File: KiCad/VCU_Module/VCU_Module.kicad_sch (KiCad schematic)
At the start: 46 parts, among them J1 5810132011, J10 12V, J12 MCU1, J13 MCU2, J14 5V, J15 3V3, J16 MCU3, J17 MCU4, J2 CN1, J3 CN2, J4 CN3, J5 MCU6, J6 CN4, J7 MCU5, J9 GND, Q1 SUD19P06-60, U3 LMR33640DDDA, U4 LMR33640DDDA

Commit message: updated pcb from sohams adjustments to schematic
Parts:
- removed S1: 100SP1T1B4M2QE, VMS_Footprints:SW_100SP1T1B4M2QE, symbol 100SP1T1B4M2QE:100SP1T1B4M2QE
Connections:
- net at CR1.1, Q1.3 (S): now also F1.1
- net +3V3 renamed 3V3
- net +5V renamed 5V
- net MCU/PA5/SPI1_SCK renamed MCU/PA5/User LED 1
- net MCU/PC9/TIM1_CH2 renamed MCU/PC9/User LED 2
- no-connect marks 3 -> 2
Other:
- sheet MCU ports: added PA5/User LED 1, PC9/User LED 2; removed PA5/SPI1_SCK, PC9/TIM1_CH2
- moved on the sheet: F1

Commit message: notes for changes from andrew
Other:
- note added: "specify in the chematic what is the fuse, what is the part number, change to fuse holder and fuse, maybe ptc fuse. probably smd holder and fuse smallest i can find change user leds remove transistor, move them next c13 between reset and ground, double check data sheet double check pa2 and pa3 are wired correctly double check pa13 and pa14 reroute traces and get pcb finalized"
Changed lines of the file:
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@@
+		)
+	)
+	(text "specify in the chematic what is the fuse, what is the part number, change to fuse holder and fuse, maybe ptc fuse. probably smd holder and fuse smallest i can find\n\nchange user leds remove transistor, move them next \n\nc13 between reset and ground, double check data sheet\n\ndouble check pa2 and pa3 are wired correctly\n\ndouble check pa13 and pa14\n\nreroute traces and get pcb finalized\n\n\n\n\n"
+		(exclude_from_sim no)
+		(at 233.68 97.536 0)
+		(effects
+			(font
+				(size 1.27 1.27)
+			)
 		)
 	)

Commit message: schematic complete with new fuse holder and specs, just need to run ERC once more PCB component placement and traces done, still need to fix some DRC Errors and check warnings Still need to ensure all components are labeled properly with no overlapping silkscreen labels
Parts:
- removed F1: Fuse, Fuse:Fuse_1206_3216Metric, symbol Device:Fuse
- removed J1: 5810132011, VMS_Footprints:CINCH_5810132011_30-pin, symbol CINCH5810132011:5810132011
- added F1: 3568, VMS_Footprints:FUSE_3568, symbol VMS_Symbols:3568
- added J1: 5810132011, VMS_Footprints:Cinch_5810132011_PCB_Header, symbol Cinch_5810132011_PCB_Header:5810132011
- J10: symbol Connector:Conn_01x02_Socket -> Connector_Generic:Conn_01x02
- J12, J13, J16, J17, J2, J3: symbol Connector:Conn_01x10_Socket -> Connector_Generic:Conn_01x10
- J14, J15, J5, J9: symbol Connector:Conn_01x04_Socket -> Connector_Generic:Conn_01x04
- J4, J6, J7: symbol Connector:Conn_01x06_Socket -> Connector_Generic:Conn_01x06
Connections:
- net VDD: now also F1.2, F1.4
- net VIN_PROTECTED: now also CR1.1, Q1.3 (S); no longer Q1.2 (D)
- net at J3.1 (Pin_1): now also J1.A11
- net at J3.10 (Pin_10): now also J1.A20
- net at J3.2 (Pin_2): now also J1.A12
- net at J3.3 (Pin_3): now also J1.A13
- net at J3.4 (Pin_4): now also J1.A14
- net at J3.5 (Pin_5): now also J1.A15
- net at J3.6 (Pin_6): now also J1.A16
- net at J3.7 (Pin_7): now also J1.A17
- net at J3.8 (Pin_8): now also J1.A18
- net at J3.9 (Pin_9): now also J1.A19
- net at J6.1 (Pin_1): now also J1.B7
- net at J6.2 (Pin_2): now also J1.B8
- net at J6.3 (Pin_3): now also J1.B9
- net at J6.4 (Pin_4): now also J1.B10
- net at J6.5 (Pin_5): now also J1.B11
- net at J6.6 (Pin_6): now also J1.B12
- net at J2.1 (Pin_1): now also J1.A1
- net at J2.10 (Pin_10): now also J1.A10
- net at J2.2 (Pin_2): now also J1.A2
- net at J2.3 (Pin_3): now also J1.A3
- net at J2.4 (Pin_4): now also J1.A4
- net at J2.5 (Pin_5): now also J1.A5
- net at J2.6 (Pin_6): now also J1.A6
- net at J2.7 (Pin_7): now also J1.A7
- net at J2.8 (Pin_8): now also J1.A8
- net at J2.9 (Pin_9): now also J1.A9
- net at J4.1 (Pin_1): now also J1.B1
- net at J4.2 (Pin_2): now also J1.B2
- net at J4.3 (Pin_3): now also J1.B3
- net at J4.4 (Pin_4): now also J1.B4
- net at J4.5 (Pin_5): now also J1.B5
- net at J4.6 (Pin_6): now also J1.B6
- new net: F1.1, F1.3, Q1.2 (D)
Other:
- note added: "Mini automotive blade fuse, 1A - 3A depending on application 36V rated"
- note removed: "specify in the chematic what is the fuse, what is the part number, change to fuse holder and fuse, maybe ptc fuse. probably smd holder and fuse smallest i can find change user leds remove transistor, move them next c13 between reset and ground, double check data sheet double check pa2 and pa3 are wired correctly double check pa13 and pa14 reroute traces and get pcb finalized"
- moved on the sheet: J10

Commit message: finished DRC checks and ERC checks in schematic and PCB, added many new components with purchase links to BOM, still need to double check previously added parts in BOM to ensure they are sufficient for higher voltage inputs
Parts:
- C11, C4: DPN 311-1869-1-ND -> 1276-7012-1-ND; MFR YAGEO -> Samsung Electro-Mechanics; MPN CC0805KKX5R8BB106 -> CL21B224KBFVPNE; Purchase Link https://www.digikey.com/en/products/detail/yageo/CC0805KKX5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 -> https://www.digikey.com/en/products/detail/samsung-electro-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
- C12, C18, C19, C20, C21, C5, C6, C7, C8, C9: DIS DigiKey -> (none); DPN 311-1869-1-ND -> (none); MFR YAGEO -> (none); MPN CC0805KKX5R8BB106 -> (none); Purchase Link https://www.digikey.com/en/products/detail/yageo/CC0805KKX5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 -> (none)
- CR1: DPN MMSZ5245B-FDICT-ND -> 3757-MMSZ5240B_R1_00001CT-ND; MFR Diodes Incorporated -> Panjit International Inc.; MPN MMSZ5240B -> MMSZ5240B_R1_00001; Purchase Link (none) -> https://www.digikey.com/en/products/detail/panjit-internati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
- F1: DIS (none) -> DigiKey; DPN (none) -> 36-3568-ND; MFR (none) -> Keystone Electronics; MPN (none) -> 3568; Purchase Link (none) -> https://www.digikey.com/en/products/detail/keystone-electro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
- J1: DIS (none) -> DigiKey; DPN (none) -> 116-1124-ND; MFR (none) -> Cinch Connectivity Solutions; MPN (none) -> 5810132011; Purchase Link (none) -> https://www.digikey.com/en/products/detail/cinch-connectivi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
- J12, J13, J16, J17, J2, J3: DIS (none) -> DigiKey; DPN (none) -> S7043-ND; MFR (none) -> Sullins Connector Solutions; MPN (none) -> PPPC101LFBN-RC; Purchase Link (none) -> https://www.digikey.com/en/products/detail/sullins-connecto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
- J4, J5, J6, J7: DIS (none) -> DigiKey; DPN (none) -> S7039-ND; MFR (none) -> Sullins Connector Solutions; MPN (none) -> PPPC061LFBN-RC; Purchase Link (none) -> https://www.digikey.com/en/products/detail/sullins-connecto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
- L1, L2: DIS (none) -> DigiKey; DPN (none) -> 1712-7-2176797-0CT-ND; MFR (none) -> TE Connectivity Passive Product; MPN (none) -> 7-2176797-0; Purchase Link (none) -> https://www.digikey.com/en/products/detail/te-connectivity-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
- Q1: DIS (none) -> DigiKey; DPN (none) -> SUD19P06-60-GE3CT-ND; MFR (none) -> Vishay Siliconix; MPN (none) -> SUD19P06-60-GE3; Purchase Link (none) -> https://www.digikey.com/en/products/detail/vishay-siliconix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
- U3, U4: DIS (none) -> DigiKey; DPN (none) -> 296-LMR33640DDDARCT-ND; MFR (none) -> Texas Instruments; MPN (none) -> LMR33640DDDAR; Purchase Link (none) -> https://www.digikey.com/en/products/detail/texas-instrument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

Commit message: finalized BOM
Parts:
- C10, C3: DPN 311-1869-1-ND -> 490-12394-1-ND; MFR YAGEO -> Murata Electronics; MPN CC0805KKX5R8BB106 -> GRT21BR61H475KE13L; Purchase Link https://www.digikey.com/en/products/detail/yageo/CC0805KKX5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 -> https://www.digikey.com/en/products/detail/murata-electroni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
- C12, C9: DIS (none) -> DigiKey; DPN (none) -> 445-6974-1-ND; MFR (none) -> TDK; MPN (none) -> CGA4J3X7S2A105K125AB; Purchase Link (none) -> https://www.digikey.com/en/products/detail/tdk/CGA4J3X7S2A1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
- C18, C5: DIS (none) -> DigiKey; DPN (none) -> 490-5825-1-ND; MFR (none) -> Murata Electronics; MPN (none) -> GCJ21BR72A104KA01L; Purchase Link (none) -> https://www.digikey.com/en/products/detail/murata-electroni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
- C19, C20, C21, C6, C7, C8: DIS (none) -> DigiKey; DPN (none) -> 4713-GMC21X5R226K16NTCT-ND; MFR (none) -> Cal-Chip Electronics, Inc.; MPN (none) -> GMC21X5R226K16NT; Purchase Link (none) -> https://www.digikey.com/en/products/detail/cal-chip-electro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
- J10: DPN S1011EC-02-ND -> S7035-ND; MPN PRPC002SAAN-RC -> PPPC021LFBN-RC; Purchase Link https://www.digikey.com/en/products/detail/sullins-connector-solutions/PRPC002SAAN-RC/2775252 -> https://www.digikey.com/en/products/detail/sullins-connector-solutions/PPPC021LFBN-RC/810174
- J14, J15, J9: DPN S1011EC-04-ND -> S7037-ND; MPN PRPC004SAAN-RC -> PPPC041LFBN-RC; Purchase Link https://www.digikey.com/en/products/detail/sullins-connector-solutions/PRPC004SAAN-RC/2775250 -> https://www.digikey.com/en/products/detail/sullins-connector-solutions/PPPC041LFBN-RC/810176
- J5: DPN S7039-ND -> S7037-ND; MPN PPPC061LFBN-RC -> PPPC041LFBN-RC; Purchase Link https://www.digikey.com/en/products/detail/sullins-connector-solutions/PPPC061LFBN-RC/810178 -> https://www.digikey.com/en/products/detail/sullins-connector-solutions/PPPC041LFBN-RC/810176
- R1: DPN 311-100KCRCT-ND -> 2019-SG73S2ATTD1003FCT-ND; MFR YAGEO -> KOA Speer Electronics, Inc.; MPN RC0805FR-07100KL -> SG73S2ATTD1003F; Purchase Link https://www.digikey.com/en/products/detail/yageo/RC0805FR-0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 -> https://www.digikey.com/en/products/detail/koa-speer-electr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
- R2, R8: DPN 311-1.00KCRCT-ND -> 2019-SG73S2ATTD1001FCT-ND; MFR YAGEO -> KOA Speer Electronics, Inc.; MPN RC0805FR-071KL -> SG73S2ATTD1001F; Purchase Link https://www.digikey.com/en/products/detail/yageo/RC0805FR-0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 -> https://www.digikey.com/en/products/detail/koa-speer-electr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
- R4, R6: DPN 311-1.00KCRCT-ND -> 2019-SG73S2ATTD1003FCT-ND; MFR YAGEO -> KOA Speer Electronics, Inc.; MPN RC0805FR-071KL -> SG73S2ATTD1003F; Purchase Link https://www.digikey.com/en/products/detail/yageo/RC0805FR-0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 -> https://www.digikey.com/en/products/detail/koa-speer-electr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
- R5: DPN 311-1.00KCRCT-ND -> 2019-RK73H2ATTD4322FCT-ND; MFR YAGEO -> KOA Speer Electronics, Inc.; MPN RC0805FR-071KL -> RK73H2ATTD4322F; Purchase Link https://www.digikey.com/en/products/detail/yageo/RC0805FR-0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 -> https://www.digikey.com/en/products/detail/koa-speer-electr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
- R7: DPN 311-1.00KCRCT-ND -> 2019-RK73H2ATTD2492FCT-ND; MFR YAGEO -> KOA Speer Electronics, Inc.; MPN RC0805FR-071KL -> RK73H2ATTD2492F; Purchase Link https://www.digikey.com/en/products/detail/yageo/RC0805FR-0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 -> https://www.digikey.com/en/products/detail/koa-speer-electr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

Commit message: final PCB fix
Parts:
- removed CR1: MMSZ5240B, VMS_Footprints:SOD123_DIO, symbol MMSZ5245B_7_F:MMSZ5245B-7-F
- added CR1: MMSZ5245B-7-F, VMS_Footprints:SOD123_DIO, symbol VMS_Symbols:MMSZ5245B-7-F
- added F2: 1A, symbol Device:Fuse
- added J18: Molex MX150 12_pin, N/A, symbol Connector_Generic:Conn_02x06_Counter_Clockwise
- added J19: Molex MX150 20_pin, N/A, symbol Connector_Generic:Conn_02x10_Counter_Clockwise
- added N1: Cinch 5810130065 Enclosure, N/A, symbol Mechanical:Housing
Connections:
- net VIN_PROTECTED: now also CR1.1
- net at Q1.1 (G), R1.1: now also CR1.2
- no-connect marks 2 -> 36
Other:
- note added: "Miniature blade fuse"

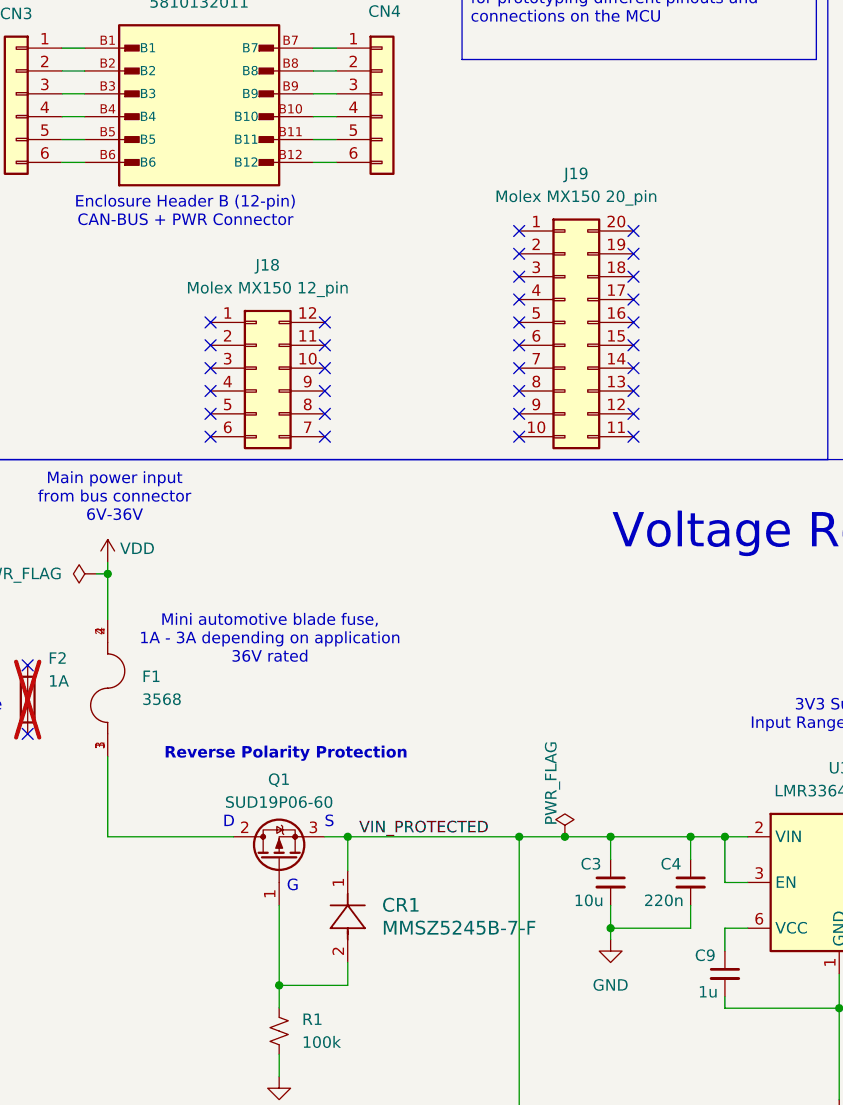
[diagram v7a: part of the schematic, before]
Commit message: updating components with AEC certified ones
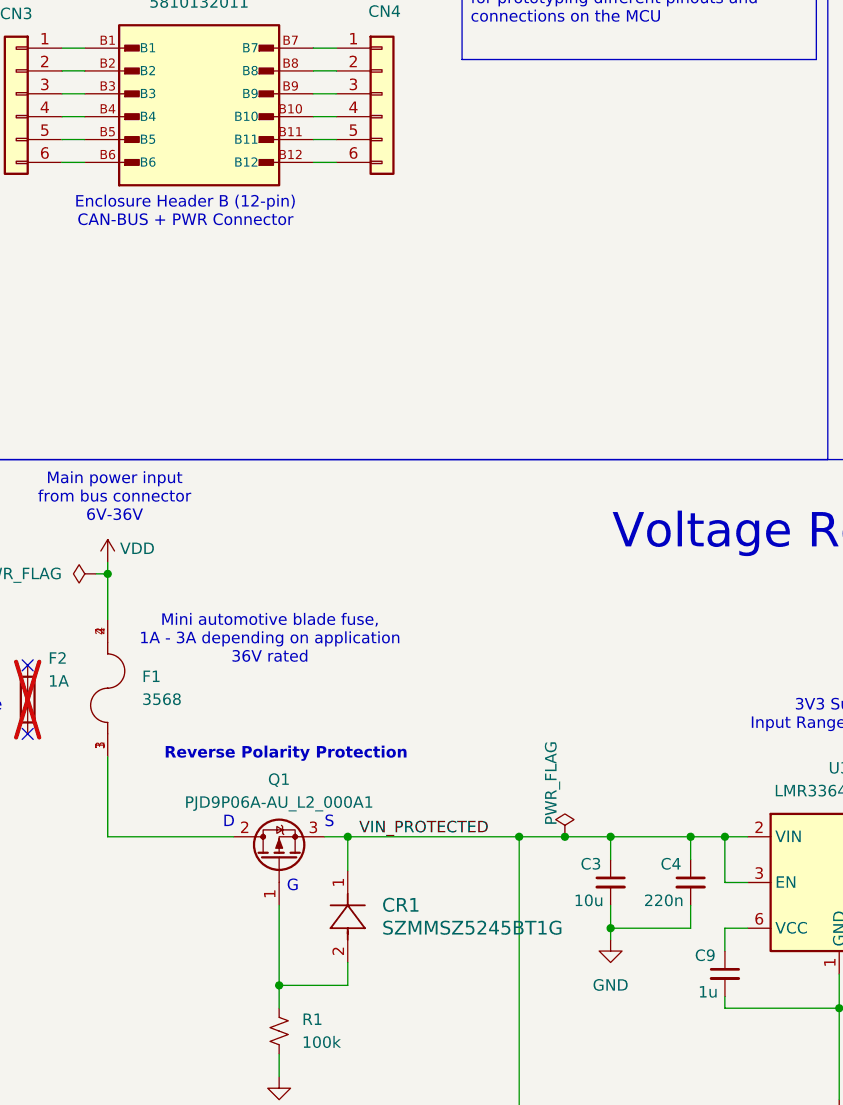
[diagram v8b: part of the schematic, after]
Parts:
- removed J18: Molex MX150 12_pin, N/A, symbol Connector_Generic:Conn_02x06_Counter_Clockwise
- removed J19: Molex MX150 20_pin, N/A, symbol Connector_Generic:Conn_02x10_Counter_Clockwise
- C10, C11, C12, C18, C3, C4, C5, C9, R1, R2, R4, R5, R6, R7, R8: Automotive Certification (none) -> AEC-Q200
- C19, C20, C21, C6, C7, C8: Automotive Certification (none) -> AEC-Q200; DPN 4713-GMC21X5R226K16NTCT-ND -> 490-GRT21BR61C226ME13KCT-ND; MFR Cal-Chip Electronics, Inc. -> Murata Electronics; MPN GMC21X5R226K16NT -> GRT21BR61C226ME13K; Purchase Link https://www.digikey.com/en/products/detail/cal-chip-electro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 -> https://www.digikey.com/en/products/detail/murata-electroni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
- CR1: value MMSZ5245B-7-F -> SZMMSZ5245BT1G; Automotive Certification (none) -> AEC-Q101; DIS (none) -> DigiKey; DPN (none) -> SZMMSZ5245BT1GOSCT-ND; MFR (none) -> onsemi; MPN (none) -> SZMMSZ5245BT1G; Purchase Link (none) -> https://www.digikey.com/en/products/detail/onsemi/SZMMSZ524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
- D1, D4: Automotive Certification (none) -> AEC-Q102; DPN 160-1179-1-ND -> 846-SMLMN2ECTT86CCT-ND; MFR Lite-On Inc. -> Rohm Semiconductor; MPN LTST-C170GKT -> SMLMN2ECTT86C; Purchase Link https://www.digikey.com/en/products/detail/liteon/LTST-C170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 -> https://www.digikey.com/en/products/detail/rohm-semiconduct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
- F1, J10, J12, J13, J14, J15, J16, J17, J2, J3, J4, J5, J6, J7, J9, U3, U4: Automotive Certification (none) -> None
- J1, N1: Automotive Certification (none) -> IP67 and IP69K
- L1, L2: Automotive Certification (none) -> AEC-Q200; DPN 1712-7-2176797-0CT-ND -> 553-AKPB002012103R3MA2CT-ND; MFR TE Connectivity Passive Product -> Pulse Electronics; MPN 7-2176797-0 -> AKPB002012103R3MA2; Purchase Link https://www.digikey.com/en/products/detail/te-connectivity-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 -> https://www.digikey.com/en/products/detail/pulse-electronic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
- Q1: value SUD19P06-60 -> PJD9P06A-AU_L2_000A1; Automotive Certification (none) -> AEC-Q101; DPN SUD19P06-60-GE3CT-ND -> 3757-PJD9P06A-AU_L2_000A1CT-ND; MFR Vishay Siliconix -> Panjit International Inc.; MPN SUD19P06-60-GE3 -> PJD9P06A-AU_L2_000A1; Purchase Link https://www.digikey.com/en/products/detail/vishay-siliconix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 -> https://www.digikey.com/en/products/detail/panjit-internati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
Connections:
- no-connect marks 36 -> 4
